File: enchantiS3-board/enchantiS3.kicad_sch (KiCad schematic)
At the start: 81 parts, among them J1 USB_C_Receptacle_USB2.0, J2 Programming Header, SW1 PTS810, SW2 PTS810, SW3 PTS810, U1 USBLC6-2P6, U12 BQ25185DLHR, U13 ICM-42670-P, U14 MAX17260SETD+T, U4 NCP167AMX330TBG, U5 CY8C4149, U8 TCAN3413DRBR, U9 NCP167AMX330TBG

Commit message: updated project to KiCad 9, added touch controller on enchantiS3 board, added canfd bus for connecting additional touch controllers
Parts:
- removed C13: 10uF, Capacitor_SMD:C_0603_1608Metric, symbol Device:C
- removed C3: 220nF, Capacitor_SMD:C_0402_1005Metric, symbol Device:C
- removed TP11: TestPoint, TestPoint:TestPoint_Pad_D1.0mm, symbol Connector:TestPoint
- removed U5: CY8C4149, TQFP50P1200X1200X160-64N:TQFP50P1200X1200X160-64N, symbol CY8C414X_TQFP64:CY8C414X_TQFP64
- added C28: 1uF, Capacitor_SMD:C_0402_1005Metric, symbol Device:C
- added C29, C30: 10uF, Capacitor_SMD:C_0402_1005Metric, symbol Device:C
- added CANFD1: JST-SH-1x04 1.0mm, ENCHANTI_connectors:JST_SMD_1.0mm-4_Vertical, symbol ENCHANTI_connectors:QWIIC-CONNECTOR
- added U3: MMC5983MA, ENCHANTI_MEMS:MMC5983MA_MEM, symbol ENCHANTI_mems:MMC5983MA
- added U5: CY8C4149AZI-S593, ENCHANTI_mcus:TQFP48_INFINEON, symbol ENCHANTI_mcus:CY8C414X_TQFP48
- C21, C23: footprint Capacitor_SMD:C_0603_1608Metric -> Capacitor_SMD:C_0402_1005Metric; Mfg Part # CL10A106KO8NNNC -> CL05A106MP8NUB8; mpn CL10A105KO8NNNC -> (none)
- R19: Mfg Part # ERJ-2RKF2201X -> ERJ-2RKF1200X
- TOUCH1: renamed from CANFD1; mpn (none) -> BM04B-SRSS-TB
- TOUCH2: footprint ffc_footprints:CON_541323262_MOL -> ENCHANTI_connectors:CON_541323262_MOL
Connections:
- net +3V3_AUX is gone; now on net 3V3_AUX: C17.1, C18.1, C59.1, C61.1, C66.1, FP1.2 (Pin_2), TOUCH1.2 (3v3), U13.5 (VDDIO), U13.8 (VDD), U8.3 (VCC), U8.5 (VIO), USER_LED1.2 (A), USER_LED2.2 (A)
- net CAN_MODE is gone; now on net GND: U8.8 (STB)
- net MSC022 is gone; now on net MSC031: TOUCH2.25 (Pin_25)
- net MSC023 is gone; now on net MSC034: TOUCH2.26 (Pin_26)
- net MSC024 is gone; now on net MSC035: TOUCH2.27 (Pin_27)
- net MSC026 is gone; now on net MSC036: TOUCH2.28 (Pin_28)
- net MSC029 is gone; now on net MSC037: TOUCH2.29 (Pin_29)
- net MSC101 is gone; now on net MSC003: TOUCH2.9 (Pin_9)
- net MSC102 is gone; now on net MSC004: TOUCH2.10 (Pin_10)
- net MSC103 is gone; now on net MSC005: TOUCH2.11 (Pin_11)
- net MSC130 is gone; now on net MSC007: TOUCH2.13 (Pin_13)
- net MSC131 is gone; now on net MSC006: TOUCH2.12 (Pin_12)
- net +3V3: now also C30.1; no longer ANG1.1 (Pin_1), ANG3.1 (Pin_1)
- net 3V3_AUX: now also ANG1.1 (Pin_1), ANG3.1 (Pin_1), C28.1, CANFD1.2 (3v3), U3.13 (VDDIO), U3.2 (VDD), U5.21 (VDDD_1), U5.39 (VDDD_2), U5.40 (VDDA)
- net BUTTON_FP: now also MCU1.6 (GPIO6/TOUCH6/ADC1_CH5)
- net CAN_H: now also D2.1 (K), CANFD1.3 (SDA); no longer D2.2 (K), TOUCH1.3 (SDA)
- net CAN_L: now also D2.2 (K), CANFD1.4 (SCL); no longer D2.1 (K), TOUCH1.4 (SCL)
- net CIPO: now also U3.5 (SPI_SDO)
- net CMOD00: now also U5.24 (P4_2)
- net CMOD01: now also U5.25 (P4_3)
- net CMOD10: now also U5.26 (P7_0)
- net CMOD11: now also U5.27 (P7_1)
- net COPI: now also U3.16 (SDA/SPI_SDI)
- net FDCAN1_RX: now also U5.30 (P0_2)
- net FDCAN1_TX: now also U5.31 (P0_3)
- net GND: now also C28.2, C29.2, C30.2, CANFD1.1 (GND), U3.11 (GND), U3.9 (GND), U5.10 (VSSD_2), U5.38 (VSSD_1), U5.41 (VSSA)
- net MSC000: now also TOUCH2.3 (Pin_3), TOUCH2.4 (Pin_4), U5.42 (P1_0)
- net MSC001: now also TOUCH2.5 (Pin_5), TOUCH2.6 (Pin_6), TOUCH2.7 (Pin_7), U5.43 (P1_1); no longer TOUCH2.3 (Pin_3)
- net MSC002: now also TOUCH2.8 (Pin_8), U5.44 (P1_2); no longer TOUCH2.4 (Pin_4)
- net MSC003: now also U5.45 (P1_3); no longer TOUCH2.5 (Pin_5)
- net MSC004: now also U5.46 (P1_4); no longer TOUCH2.6 (Pin_6)
- net MSC005: now also U5.47 (P1_5); no longer TOUCH2.7 (Pin_7)
- net MSC006: now also U5.48 (P1_6); no longer TOUCH2.8 (Pin_8)
- net MSC007: now also U5.1 (P1_7); no longer TOUCH2.16 (Pin_16)
- net MSC008: now also TOUCH2.14 (Pin_14), U5.2 (P2_0); no longer TOUCH2.17 (Pin_17)
- net MSC009: now also TOUCH2.15 (Pin_15), U5.3 (P2_1); no longer TOUCH2.18 (Pin_18)
- net MSC010: now also TOUCH2.16 (Pin_16), U5.4 (P2_2); no longer TOUCH2.19 (Pin_19)
- net MSC011: now also TOUCH2.17 (Pin_17), U5.5 (P2_3); no longer TOUCH2.20 (Pin_20)
- net MSC012: now also TOUCH2.18 (Pin_18), U5.6 (P2_4); no longer TOUCH2.21 (Pin_21)
- net MSC013: now also TOUCH2.19 (Pin_19), U5.7 (P2_5); no longer TOUCH2.22 (Pin_22)
- net MSC014: now also TOUCH2.20 (Pin_20), U5.8 (P2_6); no longer TOUCH2.23 (Pin_23)
- net MSC015: now also TOUCH2.21 (Pin_21), U5.9 (P2_7); no longer TOUCH2.24 (Pin_24)
- net MSC030: now also TOUCH2.22 (Pin_22), U5.12 (P3_0); no longer TOUCH2.31 (Pin_31)
- net MSC031: now also U5.13 (P3_1); no longer TOUCH2.30 (Pin_30)
- net MSC034: now also U5.17 (P3_4)
- net MSC035: now also U5.18 (P3_5)
- net MSC036: now also U5.19 (P3_6)
- net MSC037: now also U5.20 (P3_7)
- net MSC044: now also TOUCH2.31 (Pin_31), U5.23 (P4_1)
- net MSC045: now also TOUCH2.30 (Pin_30), U5.22 (P4_0)
- net MSC114: now also TOUCH2.24 (Pin_24), U5.28 (P0_0); no longer TOUCH2.15 (Pin_15)
- net MSC115: now also TOUCH2.23 (Pin_23), U5.29 (P0_1); no longer TOUCH2.14 (Pin_14)
- net RES: now also U5.36 (~{XRES})
- net SCLK: now also U3.1 (SCL/SPI_SCK)
- net SWCLK: now also U5.16 (P3_3)
- net SWDA: now also U5.14 (P3_2)
- net TOUCH_CIPO: now also U5.33 (P0_5)
- net TOUCH_COPI: now also U5.32 (P0_4)
- net TOUCH_CS: now also U5.35 (P0_7)
- net TOUCH_SCLK: now also U5.34 (P0_6)
- net USER_BTN: now also MCU1.4 (GPIO4/TOUCH4/ADC1_CH3)
- net VCCD: now also U5.37 (VCCD)
- net BTN_FP renamed MAG_CS
- net MAG_CS: now also U3.4 (SPI_CS); no longer MCU1.6 (GPIO6/TOUCH6/ADC1_CH5)
- net IO2 renamed MAG_INT
- net MAG_INT: now also U3.15 (INT)
- new net: C29.1, U3.10 (CAP)
- new net: CANFD1.NC1 (NC), CANFD1.NC2 (NC)
- no-connect marks 11 -> 9
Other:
- note added: "MMC59883 Magnetometer"

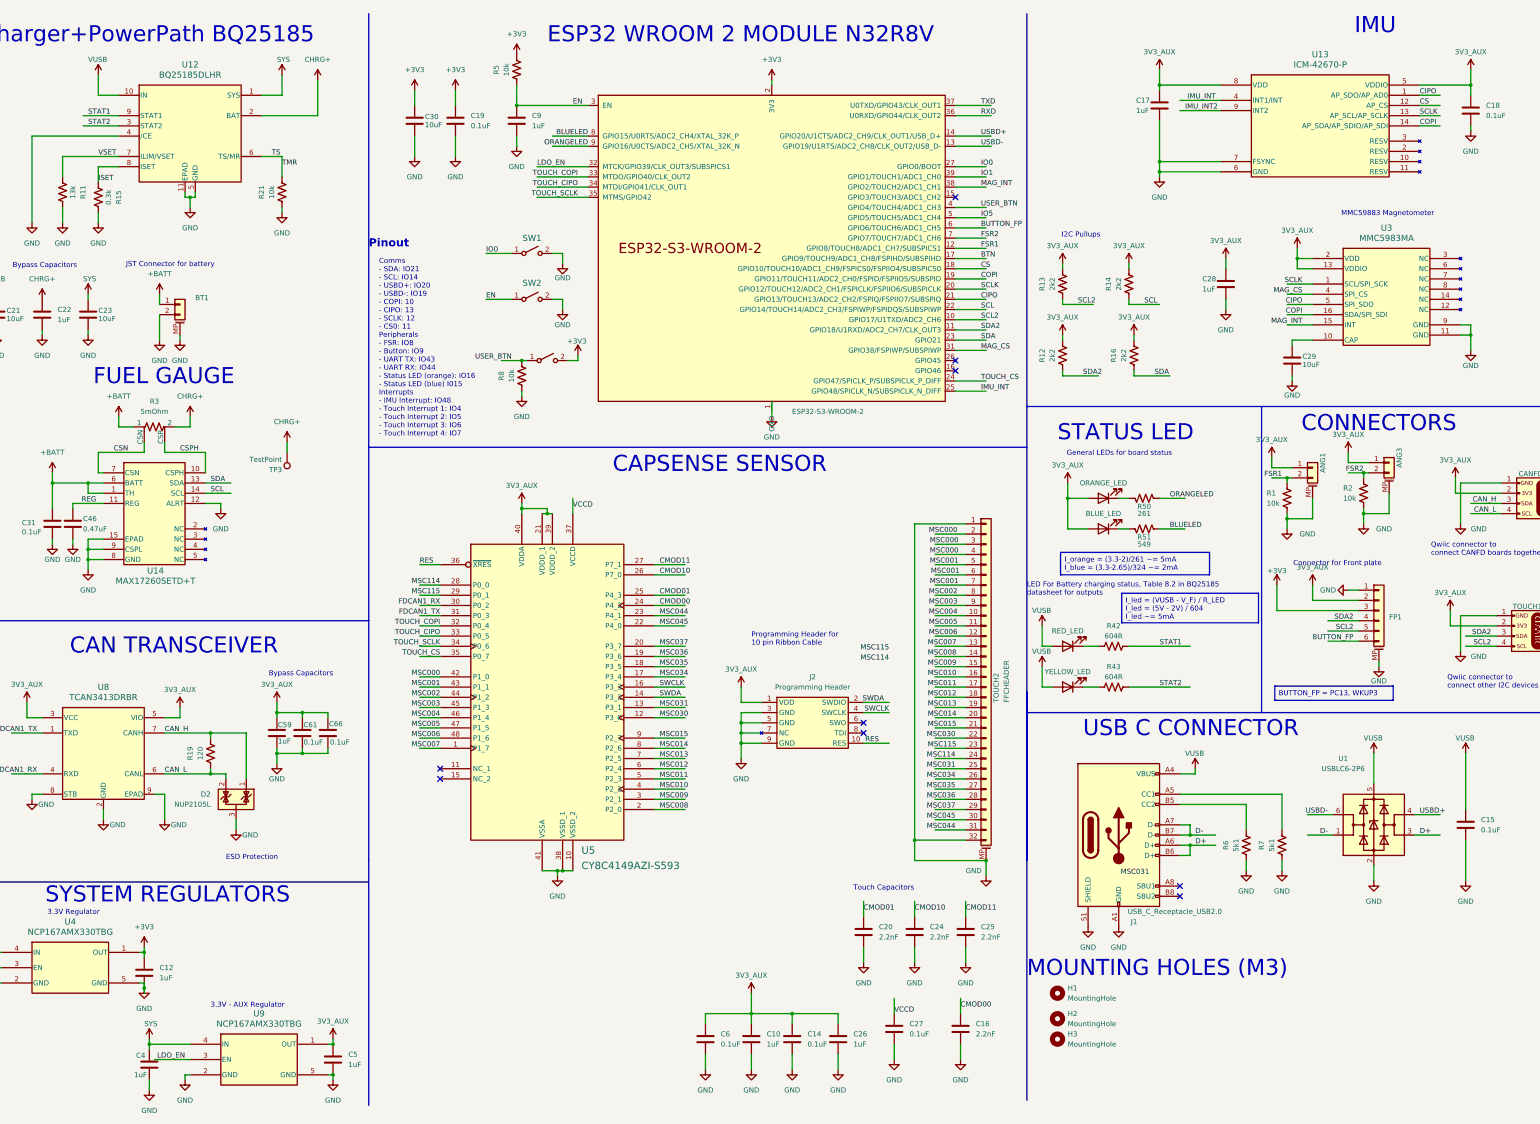
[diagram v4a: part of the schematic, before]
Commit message: removed unused library files, updated manufacturing files for latest board version, added screenshot of schematic
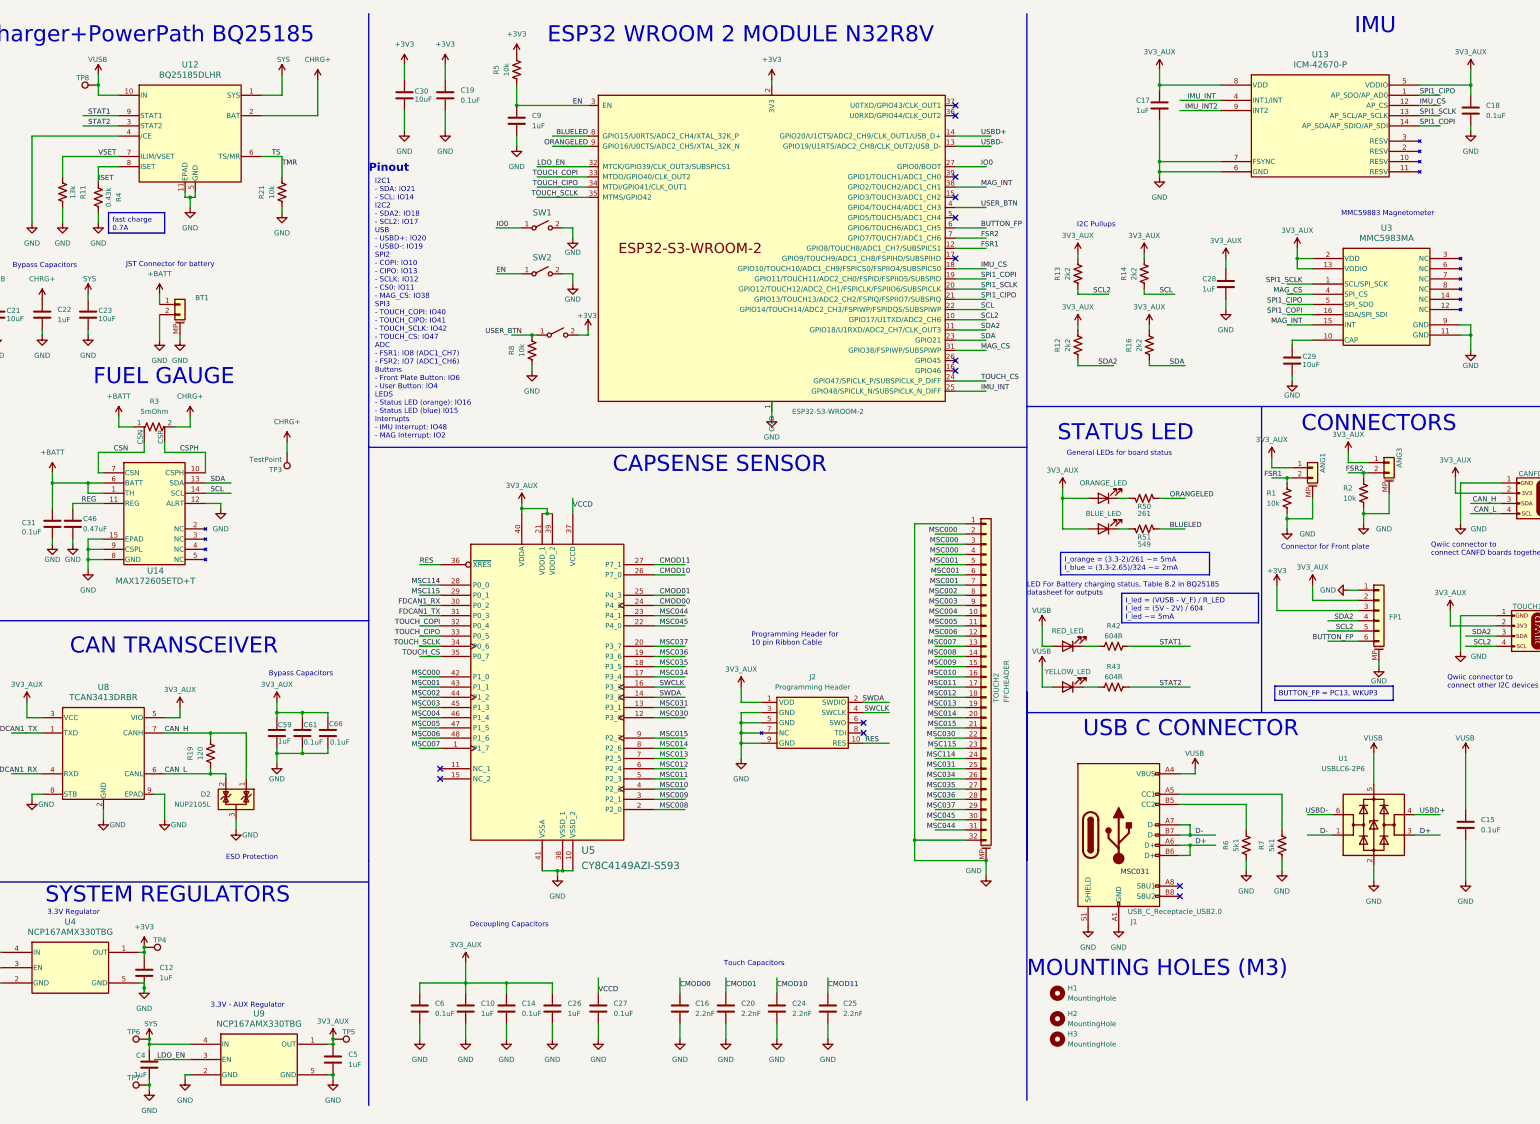
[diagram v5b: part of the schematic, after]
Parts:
- added TP4, TP5, TP6, TP7, TP8: TestPoint, TestPoint:TestPoint_Pad_D1.0mm, symbol Connector:TestPoint
- C10, C26: MPN GRM155R61C105KA12D -> (none); Manufacturer Murata Electronics -> Samsung Electro-Mechanics; Mfg Part # (none) -> CL05A105KO5NNNC
- C14, C27, C6: MPN GCM155R71C104KA55J -> (none); Manufacturer Murata Electronics -> Samsung Electro-Mechanics; Mfg Part # (none) -> CL05B104KO5NNNC
- C16, C20, C24, C25: MPN GRM155R71H222JA01J -> (none); Mfg Part # (none) -> GRM155R71H222JA01J
- R4: renamed from R15; value 0.3k -> 0.43k; Mfg Part # ERJ-2RKF3000X -> ERJ-2RKF4300X; mpn ERJ-2RKF2201X -> (none)
- TOUCH2: MPN 54132-3262 -> (none); Mfg Part # (none) -> 54132-3262
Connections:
- net +3V3: now also TP4.1
- net 3V3_AUX: now also TP5.1
- net GND: now also TP7.1
- net SYS: now also TP6.1
- net VUSB: now also TP8.1
- net BTN: no longer names the net of MCU1.17 (GPIO9/TOUCH9/ADC1_CH8/FSPIHD/SUBSPIHD)
- net CIPO renamed SPI1_CIPO
- net COPI renamed SPI1_COPI
- net CS renamed IMU_CS
- net IO1: no longer names the net of MCU1.39 (GPIO1/TOUCH1/ADC1_CH0)
- net IO5: no longer names the net of MCU1.5 (GPIO5/TOUCH5/ADC1_CH4)
- net RXD: no longer names the net of MCU1.36 (U0RXD/GPIO44/CLK_OUT2)
- net SCLK renamed SPI1_SCLK
- net TXD: no longer names the net of MCU1.37 (U0TXD/GPIO43/CLK_OUT1)
- no-connect marks 9 -> 14
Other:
- note added: "Decoupling Capacitors"
- note added: "I2C1 - SDA: IO21 - SCL: IO14 I2C2 - SDA2: IO18 - SCL2: IO17 USB - USBD+: IO20 - USBD-: IO19 SPI2 - COPI: IO10 - CIPO: IO13 - SCLK: IO12 - CS0: IO11 - MAG_CS: IO38 SPI3 - TOUCH_COPI: IO40 - TOUCH_CIPO: IO41 - TOUCH_SCLK: IO42 - TOUCH_CS: IO47 ADC - FSR1: IO8 (ADC1_CH7) - FSR2: IO7 (ADC1_CH6) Buttons - Front Plate Button: IO6 - User Button: IO4 LEDS - Status LED (orange): IO16 - Status LED (blue) I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"
- note removed: "Comms - SDA: IO21 - SCL: IO14 - USBD+: IO20 - USBD-: IO19 - COPI: 10 - CIPO: 13 - SCLK: 12 - CS0: 11 Peripherals - FSR: IO8 - Button: IO9 - UART TX: IO43 - UART RX: IO44 - Status LED (orange): IO16 - Status LED (blue) I015 Interrupts - IMU Interrupt: IO48 - Touch Interrupt 1: IO4 - Touch Interrupt 2: IO5 - Touch Interrupt 3: IO6 - Touch Interrupt 4: IO7"
- moved on the sheet: C10, C14, C16, C19, C20, C24, C25, C26, C27, C30, C6, R12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
